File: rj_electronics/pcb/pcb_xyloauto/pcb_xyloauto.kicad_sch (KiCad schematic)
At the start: 7 parts

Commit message: nc
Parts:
- added J1, J2: Conn_01x08_Pin, Connector_PinSocket_2.54mm:PinSocket_1x08_P2.54mm_Vertical, symbol Connector:Conn_01x08_Pin
- added J3: Conn_01x02_Pin, Connector_PinHeader_2.54mm:PinHeader_1x02_P2.54mm_Vertical, symbol Connector:Conn_01x02_Pin
- added U1: Sparkfun_Pro_Micro, Arduino:Sparkfun_Pro_Micro, symbol Arduino:Sparkfun_Pro_Micro
- added U2: ULN2803A, Package_DIP:DIP-18_W7.62mm_Socket, symbol Transistor_Array:ULN2803A
- C2: footprint (none) -> Capacitor_THT:CP_Radial_D10.0mm_P2.50mm
- gave numbers to parts that had none: 1
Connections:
- net GND: now also J3.1 (Pin_1), U1.23 (GND), U2.9 (GND)
- net VIN: now also J2.1 (Pin_1), J2.2 (Pin_2), J2.3 (Pin_3), J2.4 (Pin_4), J2.5 (Pin_5), J2.6 (Pin_6), J2.7 (Pin_7), J2.8 (Pin_8), J3.2 (Pin_2)
- net VOUT: now also U1.21 (VCC), U2.10 (COM)
- new net: U1.5 (D2), U2.1 (I1)
- new net: J1.8 (Pin_8), U2.11 (O8)
- new net: J1.7 (Pin_7), U2.12 (O7)
- new net: J1.6 (Pin_6), U2.13 (O6)
- new net: J1.5 (Pin_5), U2.14 (O5)
- new net: J1.4 (Pin_4), U2.15 (O4)
- new net: J1.3 (Pin_3), U2.16 (O3)
- new net: J1.2 (Pin_2), U2.17 (O2)
- new net: J1.1 (Pin_1), U2.18 (O1)
- new net: U1.6 (~D3), U2.2 (I2)
- new net: U1.7 (D4/A6), U2.3 (I3)
- new net: U1.8 (~D5), U2.4 (I4)
- new net: U1.9 (~D6/A7), U2.5 (I5)
- new net: U1.10 (D7), U2.6 (I6)
- new net: U1.11 (D8/A8), U2.7 (I7)
- new net: U1.12 (~D9/A9), U2.8 (I8)

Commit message: nc
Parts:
- added J4: Barrel_Jack, Connector Barrel Jack - Community:BarrelJack_GCT_DCJ200-10-A_Horizontal, symbol Connector - Community:Barrel_Jack
- C1: footprint Capacitor_THT:CP_Radial_D10.0mm_P2.50mm -> Capacitor_THT:CP_Radial_D7.5mm_P2.50mm
- RV1: footprint Potentiometer_THT:Potentiometer_TT_P0915N -> Potentiometer_THT:Potentiometer_Bourns_3339P_Vertical
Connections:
- net GND: now also J4.2
- net VIN: now also J4.1; no longer J2.1 (Pin_1), J2.2 (Pin_2), J2.3 (Pin_3), J2.4 (Pin_4), J2.5 (Pin_5), J2.6 (Pin_6), J2.7 (Pin_7), J2.8 (Pin_8), J3.2 (Pin_2)
- net VOUT: now also J2.1 (Pin_1), J2.2 (Pin_2), J2.3 (Pin_3), J2.4 (Pin_4), J2.5 (Pin_5), J2.6 (Pin_6), J2.7 (Pin_7), J2.8 (Pin_8), J3.2 (Pin_2)
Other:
- moved on the sheet: J1, U2

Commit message: nc
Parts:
- J4: footprint Connector Barrel Jack - Community:BarrelJack_GCT_DCJ200-10-A_Horizontal -> Connector Barrel Jack - Community:BarrelJack_Wuerth_6941xx301002
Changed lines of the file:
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@@
       (effects (font (size 1.27 1.27)))
     )
-    (property "Footprint" "Connector Barrel Jack - Community:BarrelJack_GCT_DCJ200-10-A_Horizontal" (at 116.84 31.496 0)
+    (property "Footprint" "Connector Barrel Jack - Community:BarrelJack_Wuerth_6941xx301002" (at 116.84 31.496 0)
       (effects (font (size 1.27 1.27)) hide)
     )

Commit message: nc
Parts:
- removed J1, J2: Conn_01x08_Pin, Connector_PinSocket_2.54mm:PinSocket_1x08_P2.54mm_Vertical, symbol Connector:Conn_01x08_Pin
- added J1, J5: Screw_Terminal_01x08, TerminalBlock_Phoenix:TerminalBlock_Phoenix_PT-1,5-8-3.5-H_1x08_P3.50mm_Horizontal, symbol Connector:Screw_Terminal_01x08
- R1: footprint Resistor_THT:R_Axial_DIN0414_L11.9mm_D4.5mm_P15.24mm_Horizontal -> Resistor_THT:R_Axial_DIN0207_L6.3mm_D2.5mm_P10.16mm_Horizontal
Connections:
- net VOUT: now also J5.1 (Pin_1), J5.2 (Pin_2), J5.3 (Pin_3), J5.4 (Pin_4), J5.5 (Pin_5), J5.6 (Pin_6), J5.7 (Pin_7), J5.8 (Pin_8)
- net at U2.11 (O8): now also J1.8 (Pin_8)
- net at U2.12 (O7): now also J1.7 (Pin_7)
- net at U2.13 (O6): now also J1.6 (Pin_6)
- net at U2.14 (O5): now also J1.5 (Pin_5)
- net at U2.15 (O4): now also J1.4 (Pin_4)
- net at U2.16 (O3): now also J1.3 (Pin_3)
- net at U2.17 (O2): now also J1.2 (Pin_2)
- net at U2.18 (O1): now also J1.1 (Pin_1)

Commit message: nc
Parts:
- added D3, D4, D5, D6: LED, LED_THT:LED_D5.0mm, symbol Device:LED
- added R2, R3, R4, R5: R, Resistor_THT:R_Axial_DIN0207_L6.3mm_D2.5mm_P10.16mm_Horizontal, symbol Device:R
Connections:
- net GND: now also R2.2, R3.2, R4.2, R5.2
- net LED1: now reaches U1.17 (D18/A0)
- net LED1: now also D3.2 (A)
- net LED2: now reaches U1.18 (D19/A1)
- net LED2: now also D4.2 (A)
- net LED3: now reaches U1.19 (D20/A2)
- net LED3: now also D5.2 (A)
- net LED4: now reaches U1.20 (D21/A3)
- net LED4: now also D6.2 (A)
- new net: D3.1 (K), R2.1
- new net: D5.1 (K), R4.1
- new net: D4.1 (K), R3.1
- new net: D6.1 (K), R5.1

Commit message: nc
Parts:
- RV1: footprint Potentiometer_THT:Potentiometer_Bourns_3339P_Vertical -> Potentiometer_THT:Potentiometer_Bourns_3299W_Vertical
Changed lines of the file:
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@@
       (effects (font (size 1.27 1.27)) (justify right))
     )
-    (property "Footprint" "Potentiometer_THT:Potentiometer_Bourns_3339P_Vertical" (at 45.72 57.15 0)
+    (property "Footprint" "Potentiometer_THT:Potentiometer_Bourns_3299W_Vertical" (at 45.72 57.15 0)
       (effects (font (size 1.27 1.27)) hide)
     )

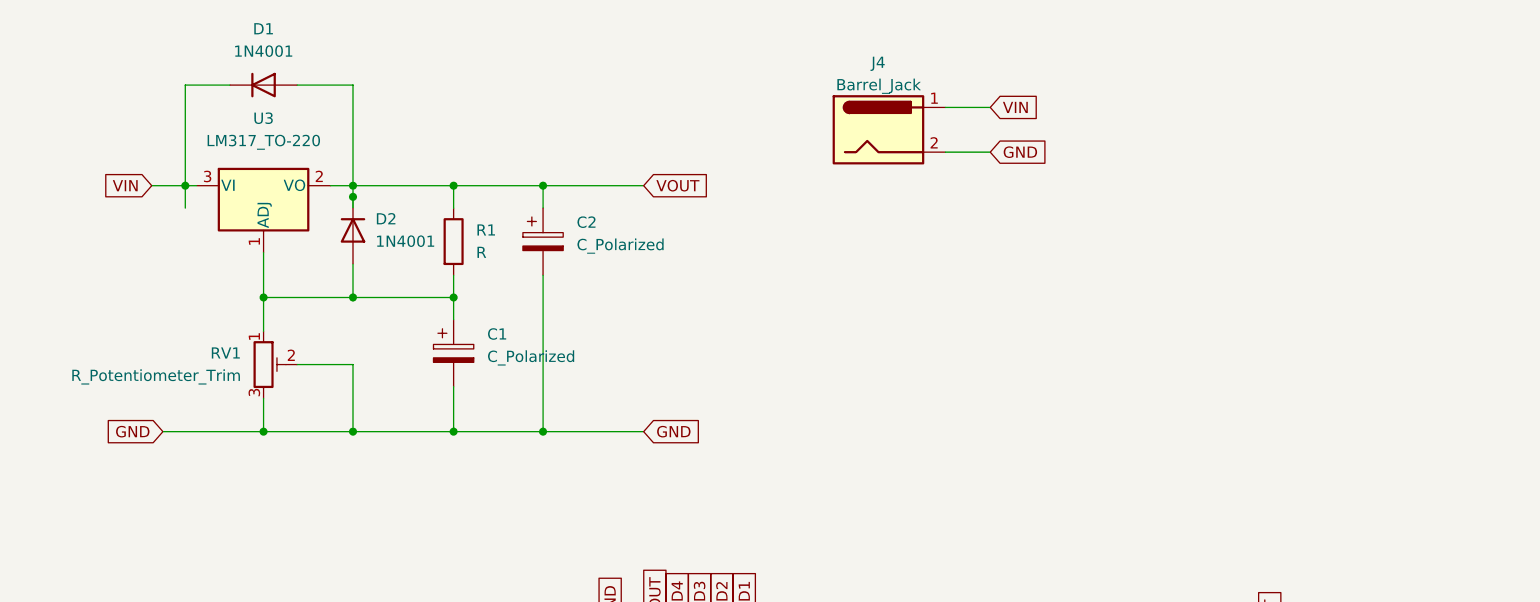
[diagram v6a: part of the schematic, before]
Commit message: LED holes
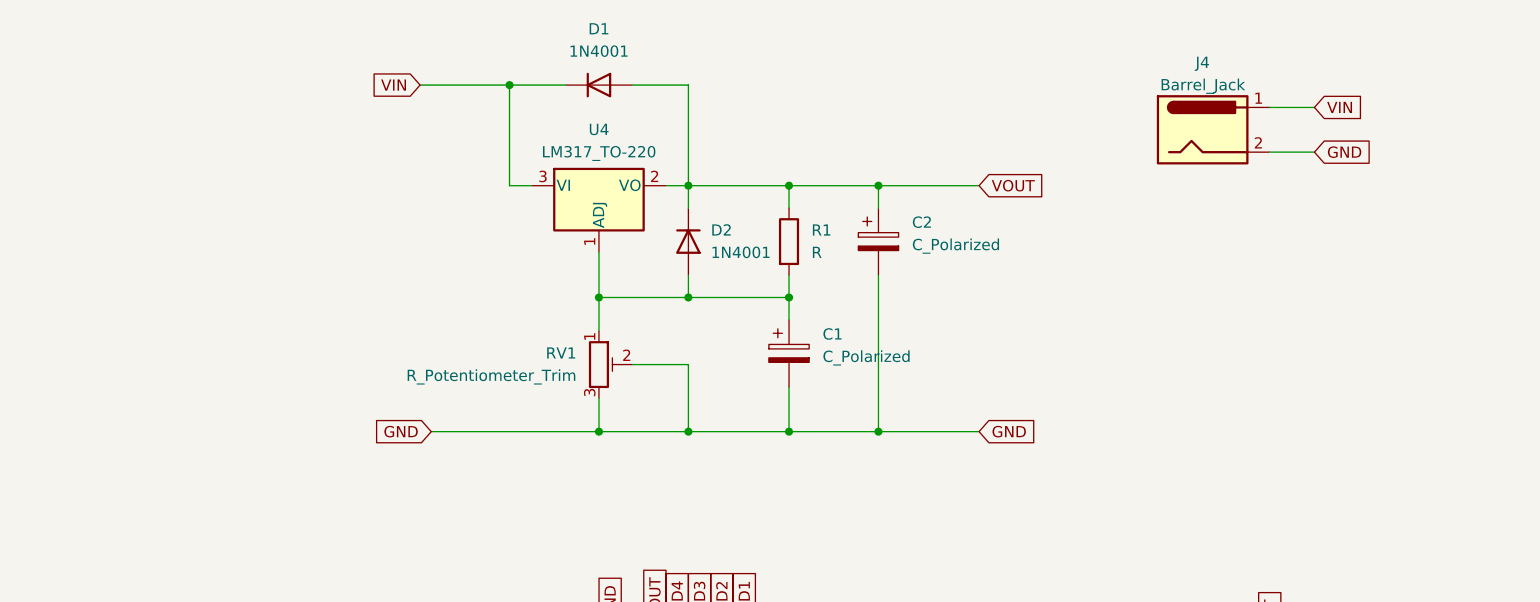
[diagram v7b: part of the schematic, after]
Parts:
- removed U3: LM317_TO-220, Package_TO_SOT_THT:TO-220-3_Vertical, symbol Regulator_Linear:LM317_TO-220
- added U4: LM317_TO-220, Package_TO_SOT_THT:TO-220-3_Vertical, symbol Regulator_Linear:LM317_TO-220
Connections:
- net VIN: now also U4.3 (VI)
- net VOUT: now also U4.2 (VO)
- net at C1.1, D2.2 (A), R1.2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: now also U4.1 (ADJ)
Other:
- moved on the sheet: C1, C2, D1, D2, J4, R1, RV1

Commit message: nc
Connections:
- no-connect marks 0 -> 10
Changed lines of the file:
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@@
   (junction (at 93.98 64.77) (diameter 0) (color 0 0 0 0)
   )
+  (junction (at 162.56 27.94) (diameter 0) (color 0 0 0 0)
+  )
   (junction (at 105.41 64.77) (diameter 0) (color 0 0 0 0)
   )
   (junction (at 83.82 64.77) (diameter 0) (color 0 0 0 0)
   )
+  (junction (at 162.56 33.02) (diameter 0) (color 0 0 0 0)
+  )
   (junction (at 105.41 36.83) (diameter 0) (color 0 0 0 0)
   )
@@
   (junction (at 73.66 25.4) (diameter 0) (color 0 0 0 0)
   )
+  (no_connect (at 87.63 129.54))
+  (no_connect (at 90.17 129.54))
+  (no_connect (at 82.55 129.54))
+  (no_connect (at 110.49 99.06))
+  (no_connect (at 105.41 99.06))
+  (no_connect (at 107.95 99.06))
+  (no_connect (at 87.63 99.06))
+  (no_connect (at 82.55 99.06))
+  (no_connect (at 85.09 129.54))
+  (no_connect (at 102.87 99.06))
   (wire (pts (xy 93.98 57.15) (xy 93.98 64.77))
     (stroke (width 0) (type default))
@@
     (stroke (width 0) (type default))
   )
-  (wire (pts (xy 160.02 33.02) (xy 165.1 33.02))
+  (wire (pts (xy 160.02 33.02) (xy 162.56 33.02))
+    (stroke (width 0) (type default))
+  )
+  (wire (pts (xy 162.56 25.4) (xy 162.56 27.94))
     (stroke (width 0) (type default))
   )
@@
     (stroke (width 0) (type default))
   )
-  (wire (pts (xy 185.42 114.3) (xy 193.04 114.3))
-    (stroke (width 0) (type default))
-  )
   (wire (pts (xy 172.72 135.89) (xy 172.72 124.46))
     (stroke (width 0) (type default))
@@
     (stroke (width 0) (type default))
   )
+  (wire (pts (xy 185.42 114.3) (xy 191.77 114.3))
+    (stroke (width 0) (type default))
+  )
   (wire (pts (xy 232.41 101.6) (xy 229.87 101.6))
     (stroke (width 0) (type default))
@@
     (stroke (width 0) (type default))
   )
+  (wire (pts (xy 162.56 33.02) (xy 162.56 35.56))
+    (stroke (width 0) (type default))
+  )
   (wire (pts (xy 95.25 139.7) (xy 165.1 139.7))
     (stroke (width 0) (type default))
@@
     (stroke (width 0) (type default))
   )
+  (wire (pts (xy 162.56 27.94) (xy 165.1 27.94))
+    (stroke (width 0) (type default))
+  )
   (wire (pts (xy 227.33 55.88) (xy 236.22 55.88))
     (stroke (width 0) (type default))
@@
     (stroke (width 0) (type default))
   )
-  (wire (pts (xy 160.02 27.94) (xy 165.1 27.94))
+  (wire (pts (xy 160.02 27.94) (xy 162.56 27.94))
     (stroke (width 0) (type default))
   )
@@
   )
   (wire (pts (xy 100.33 137.16) (xy 170.18 137.16))
+    (stroke (width 0) (type default))
+  )
+  (wire (pts (xy 162.56 33.02) (xy 165.1 33.02))
     (stroke (width 0) (type default))
   )
@@
     )
   )
-  (global_label "GND" (shape input) (at 193.04 114.3 0) (fields_autoplaced)
-    (effects (font (size 1.27 1.27)) (justify left))
-    (property "Intersheetrefs" "${INTERSHEET_REFS}" (at 199.8163 114.3 0)
+  (global_label "GND" (shape input) (at 191.77 114.3 0) (fields_autoplaced)
+    (effects (font (size 1.27 1.27)) (justify left))
+    (property "Intersheetrefs" "${INTERSHEET_REFS}" (at 198.5463 114.3 0)
       (effects (font (size 1.27 1.27)) (justify left) hide)
     )
@@
     )
   )
+  (symbol (lib_id "power:GND") (at 162.56 35.56 0) (unit 1)
+    (in_bom yes) (on_board yes) (dnp no) (fields_autoplaced)
+    (property "Reference" "#PWR01" (at 162.56 41.91 0)
+      (effects (font (size 1.27 1.27)) hide)
+    )
+    (property "Value" "GND" (at 162.56 40.64 0)
+      (effects (font (size 1.27 1.27)))
+    )
+    (property "Footprint" "" (at 162.56 35.56 0)
+      (effects (font (size 1.27 1.27)) hide)
+    )
+    (property "Datasheet" "" (at 162.56 35.56 0)
+      (effects (font (size 1.27 1.27)) hide)
+    )
+    (pin "1")
+    (instances
+      (project "pcb_xyloauto"
+        (path "/720c51e5-653f-4a9c-b040-f99d22f2970d"
+          (reference "#PWR01") (unit 1)
+        )
+      )
+    )
+  )
   (symbol (lib_id "Device:C_Polarized") (at 115.57 43.18 0) (unit 1)
     (in_bom yes) (on_board yes) (dnp no) (fields_autoplaced)
@@
         )
       )
+    )
+  )
+  (symbol (lib_id "power:PWR_FLAG") (at 162.56 25.4 0) (unit 1)
+    (in_bom yes) (on_board yes) (dnp no) (fields_autoplaced)
+    (property "Reference" "#FLG01" (at 162.56 23.495 0)
+      (effects (font (size 1.27 1.27)) hide)
+    )
+    (property "Value" "PWR_FLAG" (at 162.56 20.32 0)
+      (effects (font (size 1.27 1.27)))
+    )
+    (property "Footprint" "" (at 162.56 25.4 0)
+      (effects (font (size 1.27 1.27)) hide)
+    )
+    (property "Datasheet" "~" (at 162.56 25.4 0)
+      (effects (font (size 1.27 1.27)) hide)
+    )
+    (pin "1")
+    (instances
+      (project "pcb_xyloauto"
+        (path "/720c51e5-653f-4a9c-b040-f99d22f2970d"
+          (reference "#FLG01") (unit 1)
+        )
+      )
